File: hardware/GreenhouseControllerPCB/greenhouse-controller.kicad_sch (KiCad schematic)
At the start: 70 parts, among them J1 Motor 2, J10 ALARM contact, J11 AC-Mains, J12 DM1AA-SF-PEJ72, J13 MODBUS RS485 S200, J2 24V in, J3 I2C Display, J4 Keypad, J6 Motor 3, J7 Motor 1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

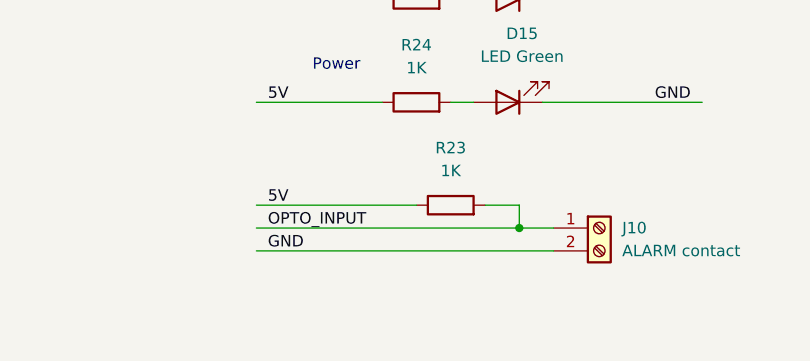
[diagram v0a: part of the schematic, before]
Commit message: rc.1.5.5 — IO MUX pin glitch filter on GPIO42 (motor-alarm EMI defense)
Software complement to the 1.8 kΩ shunt resistor installed on unit
5C88 (2026-05-29) across the alarm input pad. The shunt sets a
current-amplitude floor that EMI must overcome to flip the GPIO
through threshold (lowering source impedance from 1 kΩ to ~643 Ω);
this filter sets a duration floor at the IO MUX (~25 ns) before any
interrupt is raised.

ESP-IDF's gpio_new_pin_glitch_filter() inserts a 2-IO-MUX-clock-cycle
filter into the input path between the pad and the GPIO matrix
interrupt logic. Sub-25 ns pulses — the bulk of capacitively-coupled
EMI on long unterminated cables — are dropped at silicon, costing
zero CPU cycles. Genuine mechanical alarm-contact transitions settle
in ≥ 1 ms so they pass through unaffected.

The four-layer defense stack now in place on the alarm pipeline:

  hardware divider  → amplitude floor (~mA injection required)   [HW]
  pin glitch filter → duration floor (≥ 25 ns to register)       [rc.1.5.5]
  ISR rate-limit    → ≥ 5 ms between accepted edges              [rc.1.5.3]
  task debounce     → re-read live pin 75 ms after edge          [rc.1.4 baseline]

For an EMI event to now produce a spurious alarm it must clear all
four floors simultaneously. Real alarm transitions clear them by
construction.

Failure to create the filter is non-fatal — the rate-limit + task
debounce remain in place, just less robustly; a warning is logged
and operation continues. On success: ESP_LOGI emits
"GPIO42 pin glitch filter enabled (~25 ns IO MUX drop)" at boot.

Build + OTA verified on unit 5C88 (192.168.20.150):
  fw_ver         = 2.0.0-rc.1.5.5
  asset_version  = 2.0.0-rc.1.5.5
  bank=A accepted=true (past T1's 30 s healthy mark)
  no rollback, no coredump

Flash: 64.7 % → 64.8 % (+1504 B — IDF gpio_filter component).
RAM:   18.9 % unchanged (+8 B handle pointer in .bss).

Added pull down resistor to PCB for alarm input tom meet 3,3V compliance of GPIO and mitigate EMI on input.
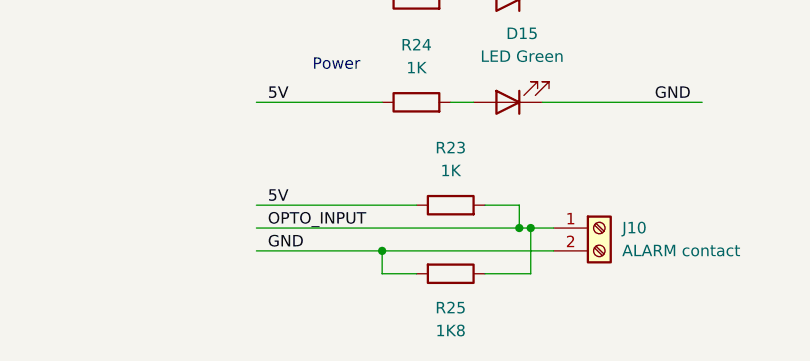
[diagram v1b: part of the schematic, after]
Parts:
- added R25: 1K8, Resistor_SMD:R_1206_3216Metric_Pad1.30x1.75mm_HandSolder, symbol Device:R
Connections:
- net GND: now also R25.2
- net OPTO_INPUT: now also R25.1
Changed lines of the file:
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@@
 	)
 	(junction
+		(at 208.28 269.24)
+		(diameter 0)
+		(color 0 0 0 0)
+	)
+	(junction
 		(at 326.39 60.96)
 		(diameter 0)
@@
 	)
 	(junction
+		(at 191.77 271.78)
+		(diameter 0)
+		(color 0 0 0 0)
+	)
+	(junction
 		(at 246.38 60.96)
 		(diameter 0)
@@
 	(wire
 		(pts
+			(xy 191.77 271.78) (xy 210.82 271.78)
+		)
+		(stroke
+			(width 0)
+			(type default)
+		)
+	)
+	(wire
+		(pts
 			(xy 81.28 80.01) (xy 102.87 80.01)
 		)
@@
 	(wire
 		(pts
+			(xy 208.28 269.24) (xy 210.82 269.24)
+		)
+		(stroke
+			(width 0)
+			(type default)
+		)
+	)
+	(wire
+		(pts
 			(xy 177.8 255.27) (xy 191.77 255.27)
 		)
@@
 	(wire
 		(pts
+			(xy 208.28 274.32) (xy 208.28 269.24)
+		)
+		(stroke
+			(width 0)
+			(type default)
+		)
+	)
+	(wire
+		(pts
 			(xy 339.09 140.97) (xy 339.09 143.51)
 		)
@@
 	(wire
 		(pts
+			(xy 195.58 274.32) (xy 191.77 274.32)
+		)
+		(stroke
+			(width 0)
+			(type default)
+		)
+	)
+	(wire
+		(pts
 			(xy 133.35 82.55) (xy 135.89 82.55)
 		)
@@
 	(wire
 		(pts
+			(xy 203.2 274.32) (xy 208.28 274.32)
+		)
+		(stroke
+			(width 0)
+			(type default)
+		)
+	)
+	(wire
+		(pts
 			(xy 135.89 85.09) (xy 154.94 85.09)
 		)
@@
 	(wire
 		(pts
-			(xy 207.01 269.24) (xy 210.82 269.24)
+			(xy 207.01 269.24) (xy 208.28 269.24)
 		)
 		(stroke
@@
 	(wire
 		(pts
-			(xy 177.8 271.78) (xy 210.82 271.78)
+			(xy 177.8 271.78) (xy 191.77 271.78)
 		)
 		(stroke
@@
 	(wire
 		(pts
+			(xy 191.77 274.32) (xy 191.77 271.78)
+		)
+		(stroke
+			(width 0)
+			(type default)
+		)
+	)
+	(wire
+		(pts
 			(xy 339.09 60.96) (xy 326.39 60.96)
 		)
@@
 					(unit 1)
 				)
+			)
+		)
+	)
+	(symbol
+		(lib_id "Device:R")
+		(at 199.39 274.32 270)
+		(unit 1)
+		(body_style 1)
+		(exclude_from_sim no)
+		(in_bom yes)
+		(on_board yes)
+		(in_pos_files yes)
+		(dnp no)
+		(property "Reference" "R25"
+			(at 199.39 278.13 90)
+			(show_name no)
+			(do_not_autoplace no)
+			(effects
+				(font
+					(size 1.27 1.27)
+				)
+			)
+		)
+		(property "Value" "1K8"
+			(at 199.39 280.67 90)
+			(show_name no)
+			(do_not_autoplace no)
+			(effects
+				(font
+					(size 1.27 1.27)
+				)
+			)
+		)
+		(property "Footprint" "Resistor_SMD:R_1206_3216Metric_Pad1.30x1.75mm_HandSolder"
+			(at 199.39 272.542 90)
+			(hide yes)
+			(show_name no)
+			(do_not_autoplace no)
+			(effects
+				(font
+					(size 1.27 1.27)
+				)
+			)
+		)
+		(property "Datasheet" ""
+			(at 199.39 274.32 0)
+			(hide yes)
+			(show_name no)
+			(do_not_autoplace no)
+			(effects
+				(font
+					(size 1.27 1.27)
+				)
+			)
+		)
+		(property "Description" "Resistor"
+			(at 199.39 274.32 0)
+			(hide yes)
+			(show_name no)
+			(do_not_autoplace no)
+			(effects
+				(font
+					(size 1.27 1.27)
+				)
+			)
+		)
+		(pin "1"
+		)
+		(pin "2"
+		)
+		(instances
+			(project "greenhouse-controller"
+				(path "/2be5eb1b-bfdc-4766-9909-5178f7452cd9"
+					(reference "R25")
+					(unit 1)
+				)
